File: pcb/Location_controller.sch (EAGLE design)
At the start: 41 parts, among them IC1 LIS302DL, X1 22-23-2021

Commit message: Further pcb layout routing
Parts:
- added DRN_POWER, RCM_POWER: (no value), pinhead:PINHD-1X2
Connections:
- removed net N$10: C9.1, POWER.1, REG.VOUT
- new net IN_3V: C8.1, POWER.2, REG.ENABLE, REG.VIN
- new net N$5: POWER.1, X1-1.S
- net GND: now also DRN_POWER.1, RCM_POWER.1
- net N$4: now also DRN_POWER.2, POWER.3; no longer C8.1, REG.ENABLE, REG.VIN, X1-1.S
- net VDD: now also C9.1, REG.VOUT; no longer POWER.2
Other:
- note added: "BATTERY"
- note added: "DRONE POWER"
- moved on the sheet: POWER, X1-1, X1-2

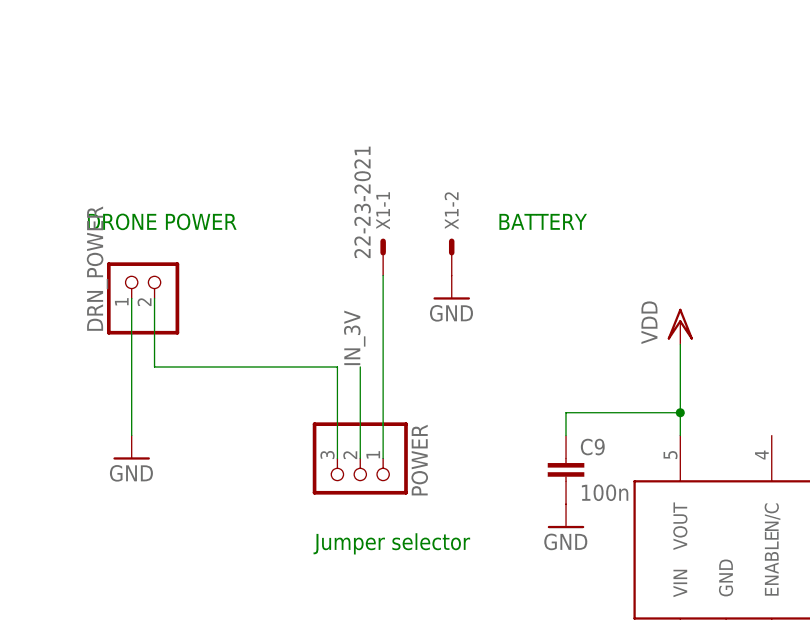
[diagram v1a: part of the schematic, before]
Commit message: Add barrel DC-jack to pcb
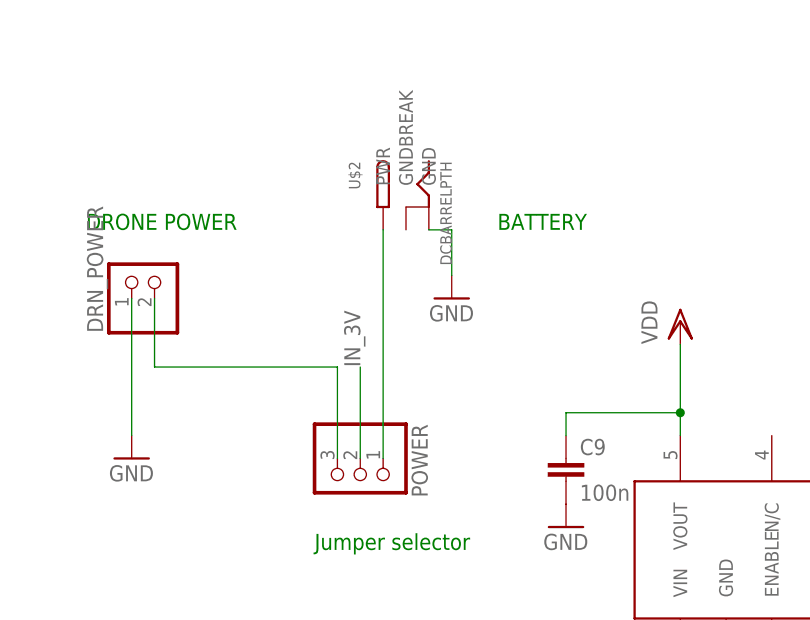
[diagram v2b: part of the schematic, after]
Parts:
- removed X1: 22-23-2021, con-molex:22-23-2021
- added U$2: DCBARRELPTH, BaseApp:DCBARRELPTH
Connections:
- net GND: now also U$2.GND; no longer X1-2.S
- net N$5: now also U$2.PWR; no longer X1-1.S
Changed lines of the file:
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@@
 <part name="C9" library="eagle-ltspice" deviceset="C" device="" value="100n"/>
 <part name="GND13" library="supply1" deviceset="GND" device=""/>
-<part name="X1" library="con-molex" deviceset="22-23-2021" device=""/>
 <part name="GND14" library="supply1" deviceset="GND" device=""/>
 <part name="GND15" library="supply1" deviceset="GND" device=""/>
@@
 <part name="RCM_POWER" library="pinhead" deviceset="PINHD-1X2" device=""/>
 <part name="GND19" library="supply1" deviceset="GND" device=""/>
+<part name="U$2" library="BaseApp" deviceset="DCBARREL" device="PTH"/>
 </parts>
 <sheets>
@@
 <instance part="C9" gate="G$1" x="-55.88" y="101.6"/>
 <instance part="GND13" gate="1" x="-55.88" y="93.98"/>
-<instance part="X1" gate="-1" x="-76.2" y="124.46" rot="R90"/>
-<instance part="X1" gate="-2" x="-68.58" y="124.46" rot="R90"/>
 <instance part="GND14" gate="1" x="-68.58" y="119.38"/>
 <instance part="GND15" gate="1" x="10.16" y="66.04"/>
@@
 <instance part="RCM_POWER" gate="G$1" x="-154.94" y="129.54" rot="R90"/>
 <instance part="GND19" gate="1" x="-157.48" y="119.38"/>
+<instance part="U$2" gate="G$1" x="-73.66" y="132.08" rot="MR270"/>
 </instances>
 <busses>
@@
 </segment>
 <segment>
-<pinref part="X1" gate="-2" pin="S"/>
-<pinref part="GND14" gate="1" pin="GND"/>
-</segment>
-<segment>
 <pinref part="GND18" gate="1" pin="GND"/>
 <pinref part="DRN_POWER" gate="G$1" pin="1"/>
@@
 <pinref part="GND19" gate="1" pin="GND"/>
 <wire x1="-157.48" y1="127" x2="-157.48" y2="121.92" width="0.1524" layer="91"/>
+</segment>
+<segment>
+<pinref part="U$2" gate="G$1" pin="GND"/>
+<pinref part="GND14" gate="1" pin="GND"/>
+<wire x1="-71.12" y1="127" x2="-68.58" y2="127" width="0.1524" layer="91"/>
+<wire x1="-68.58" y1="127" x2="-68.58" y2="121.92" width="0.1524" layer="91"/>
 </segment>
 </net>
@@
 <net name="N$5" class="0">
 <segment>
-<pinref part="X1" gate="-1" pin="S"/>
 <pinref part="POWER" gate="A" pin="1"/>
-<wire x1="-76.2" y1="121.92" x2="-76.2" y2="101.6" width="0.1524" layer="91"/>
-</segment>
-</net>
+<wire x1="-76.2" y1="127" x2="-76.2" y2="101.6" width="0.1524" layer="91"/>
+<pinref part="U$2" gate="G$1" pin="PWR"/>
+</segment>
+</net>

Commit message: Finish pcb routing
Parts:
- added JP1, JP3: (no value), pinhead:PINHD-1X6
- JP2: device pinhead:PINHD-1X20 -> pinhead:PINHD-1X6
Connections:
- net GND: now also JP1.1; no longer JP2.15
- net IN_3V: now also RCM_POWER.2
- net USART2_RX: now also JP1.5; no longer JP2.19
- net USART2_TX: now also JP1.4; no longer JP2.18
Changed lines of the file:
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@@
 <grid distance="0.1" unitdist="inch" unit="inch" style="lines" multiple="1" display="no" altdistance="0.01" altunitdist="inch" altunit="inch"/>
 <layers>
-<layer number="1" name="Top" color="4" fill="1" visible="no" active="no"/>
-<layer number="16" name="Bottom" color="1" fill="1" visible="no" active="no"/>
-<layer number="17" name="Pads" color="2" fill="1" visible="no" active="no"/>
-<layer number="18" name="Vias" color="2" fill="1" visible="no" active="no"/>
-<layer number="19" name="Unrouted" color="6" fill="1" visible="no" active="no"/>
-<layer number="20" name="Dimension" color="15" fill="1" visible="no" active="no"/>
-<layer number="21" name="tPlace" color="7" fill="1" visible="no" active="no"/>
-<layer number="22" name="bPlace" color="7" fill="1" visible="no" active="no"/>
-<layer number="23" name="tOrigins" color="15" fill="1" visible="no" active="no"/>
-<layer number="24" name="bOrigins" color="15" fill="1" visible="no" active="no"/>
-<layer number="25" name="tNames" color="7" fill="1" visible="no" active="no"/>
-<layer number="26" name="bNames" color="7" fill="1" visible="no" active="no"/>
-<layer number="27" name="tValues" color="7" fill="1" visible="no" active="no"/>
-<layer number="28" name="bValues" color="7" fill="1" visible="no" active="no"/>
+<layer number="1" name="Top" color="4" fill="1" visible="yes" active="no"/>
+<layer number="16" name="Bottom" color="1" fill="1" visible="yes" active="no"/>
+<layer number="17" name="Pads" color="2" fill="1" visible="yes" active="no"/>
+<layer number="18" name="Vias" color="2" fill="1" visible="yes" active="no"/>
+<layer number="19" name="Unrouted" color="6" fill="1" visible="yes" active="no"/>
+<layer number="20" name="Dimension" color="15" fill="1" visible="yes" active="no"/>
+<layer number="21" name="tPlace" color="7" fill="1" visible="yes" active="no"/>
+<layer number="22" name="bPlace" color="7" fill="1" visible="yes" active="no"/>
+<layer number="23" name="tOrigins" color="15" fill="1" visible="yes" active="no"/>
+<layer number="24" name="bOrigins" color="15" fill="1" visible="yes" active="no"/>
+<layer number="25" name="tNames" color="7" fill="1" visible="yes" active="no"/>
+<layer number="26" name="bNames" color="7" fill="1" visible="yes" active="no"/>
+<layer number="27" name="tValues" color="7" fill="1" visible="yes" active="no"/>
+<layer number="28" name="bValues" color="7" fill="1" visible="yes" active="no"/>
 <layer number="29" name="tStop" color="7" fill="3" visible="no" active="no"/>
 <layer number="30" name="bStop" color="7" fill="6" visible="no" active="no"/>
@@
 <layer number="35" name="tGlue" color="7" fill="4" visible="no" active="no"/>
 <layer number="36" name="bGlue" color="7" fill="5" visible="no" active="no"/>
-<layer number="37" name="tTest" color="7" fill="1" visible="no" active="no"/>
-<layer number="38" name="bTest" color="7" fill="1" visible="no" active="no"/>
+<layer number="37" name="tTest" color="7" fill="1" visible="yes" active="no"/>
+<layer number="38" name="bTest" color="7" fill="1" visible="yes" active="no"/>
 <layer number="39" name="tKeepout" color="4" fill="11" visible="no" active="no"/>
 <layer number="40" name="bKeepout" color="1" fill="11" visible="no" active="no"/>
@@
 <layer number="44" name="Drills" color="7" fill="1" visible="no" active="no"/>
 <layer number="45" name="Holes" color="7" fill="1" visible="no" active="no"/>
-<layer number="46" name="Milling" color="3" fill="1" visible="no" active="no"/>
-<layer number="47" name="Measures" color="7" fill="1" visible="no" active="no"/>
-<layer number="48" name="Document" color="7" fill="1" visible="no" active="no"/>
-<layer number="49" name="Reference" color="7" fill="1" visible="no" active="no"/>
-<layer number="50" name="dxf" color="7" fill="1" visible="no" active="no"/>
-<layer number="51" name="tDocu" color="7" fill="1" visible="no" active="no"/>
-<layer number="52" name="bDocu" color="7" fill="1" visible="no" active="no"/>
-<layer number="53" name="tGND_GNDA" color="7" fill="9" visible="no" active="no"/>
-<layer number="54" name="bGND_GNDA" color="1" fill="9" visible="no" active="no"/>
-<layer number="56" name="wert" color="7" fill="1" visible="no" active="no"/>
-<layer number="57" name="tCAD" color="10" fill="1" visible="no" active="no"/>
-<layer number="58" name="bCAD" color="11" fill="1" visible="no" active="no"/>
+<layer number="46" name="Milling" color="3" fill="1" visible="yes" active="no"/>
+<layer number="47" name="Measures" color="7" fill="1" visible="yes" active="no"/>
+<layer number="48" name="Document" color="7" fill="1" visible="yes" active="no"/>
+<layer number="49" name="Reference" color="7" fill="1" visible="yes" active="no"/>
+<layer number="50" name="dxf" color="7" fill="1" visible="yes" active="no"/>
+<layer number="51" name="tDocu" color="7" fill="1" visible="yes" active="no"/>
+<layer number="52" name="bDocu" color="7" fill="1" visible="yes" active="no"/>
+<layer number="53" name="tGND_GNDA" color="7" fill="9" visible="yes" active="no"/>
+<layer number="54" name="bGND_GNDA" color="1" fill="9" visible="yes" active="no"/>
+<layer number="56" name="wert" color="7" fill="1" visible="yes" active="no"/>
+<layer number="57" name="tCAD" color="10" fill="1" visible="yes" active="no"/>
+<layer number="58" name="bCAD" color="11" fill="1" visible="yes" active="no"/>
 <layer number="91" name="Nets" color="2" fill="1" visible="yes" active="yes"/>
 <layer number="92" name="Busses" color="1" fill="1" visible="yes" active="yes"/>
@@
 <part name="GND6" library="supply1" deviceset="GND" device=""/>
 <part name="POWER" library="pinhead" deviceset="PINHD-1X3" device=""/>
-<part name="JP2" library="pinhead" deviceset="PINHD-1X20" device=""/>
 <part name="GND7" library="supply1" deviceset="GND" device=""/>
 <part name="VDD2" library="supply1" deviceset="VDD" device=""/>
@@
 <part name="GND19" library="supply1" deviceset="GND" device=""/>
 <part name="U$2" library="BaseApp" deviceset="DCBARREL" device="PTH"/>
+<part name="JP1" library="pinhead" deviceset="PINHD-1X6" device=""/>
+<part name="JP2" library="pinhead" deviceset="PINHD-1X6" device=""/>
+<part name="JP3" library="pinhead" deviceset="PINHD-1X6" device=""/>
 </parts>
 <sheets>
@@
 <instance part="GND6" gate="1" x="27.94" y="142.24" rot="R180"/>
 <instance part="POWER" gate="A" x="-78.74" y="99.06" rot="R270"/>
-<instance part="JP2" gate="A" x="-50.8" y="-60.96" rot="R90"/>
-<instance part="GND7" gate="1" x="-38.1" y="-81.28"/>
+<instance part="GND7" gate="1" x="-40.64" y="-81.28"/>
 <instance part="VDD2" gate="G$1" x="152.4" y="-7.62" rot="R270"/>
 <instance part="R5" gate="G$1" x="139.7" y="-7.62" rot="R180"/>
@@
 <instance part="GND19" gate="1" x="-157.48" y="119.38"/>
 <instance part="U$2" gate="G$1" x="-73.66" y="132.08" rot="MR270"/>
+<instance part="JP1" gate="A" x="-33.02" y="-60.96" rot="R90"/>
+<instance part="JP2" gate="A" x="-55.88" y="-60.96" rot="R90"/>
+<instance part="JP3" gate="A" x="-78.74" y="-60.96" rot="R90"/>
 </instances>
 <busses>
@@
 </segment>
 <segment>
-<pinref part="JP2" gate="A" pin="15"/>
-<wire x1="-38.1" y1="-63.5" x2="-38.1" y2="-78.74" width="0.1524" layer="91"/>
-<pinref part="GND7" gate="1" pin="GND"/>
-</segment>
-<segment>
 <pinref part="SWD" gate="A" pin="3"/>
 <pinref part="GND17" gate="1" pin="GND"/>
@@
 <wire x1="-71.12" y1="127" x2="-68.58" y2="127" width="0.1524" layer="91"/>
 <wire x1="-68.58" y1="127" x2="-68.58" y2="121.92" width="0.1524" layer="91"/>
+</segment>
+<segment>
+<pinref part="GND7" gate="1" pin="GND"/>
+<pinref part="JP1" gate="A" pin="1"/>
+<wire x1="-40.64" y1="-78.74" x2="-40.64" y2="-63.5" width="0.1524" layer="91"/>
 </segment>
 </net>
@@
 </segment>
 <segment>
-<pinref part="JP2" gate="A" pin="18"/>
-<wire x1="-30.48" y1="-63.5" x2="-30.48" y2="-78.74" width="0.1524" layer="91"/>
-<label x="-30.48" y="-83.82" size="1.778" layer="95" rot="R90"/>
+<pinref part="JP1" gate="A" pin="4"/>
+<wire x1="-33.02" y1="-63.5" x2="-33.02" y2="-78.74" width="0.1524" layer="91"/>
+<label x="-33.02" y="-78.74" size="1.778" layer="95" rot="R90"/>
 </segment>
 </net>
@@
 </segment>
 <segment>
-<pinref part="JP2" gate="A" pin="19"/>
-<wire x1="-27.94" y1="-63.5" x2="-27.94" y2="-78.74" width="0.1524" layer="91"/>
-<label x="-25.4" y="-83.82" size="1.778" layer="95" rot="R90"/>
+<pinref part="JP1" gate="A" pin="5"/>
+<wire x1="-30.48" y1="-63.5" x2="-30.48" y2="-78.74" width="0.1524" layer="91"/>
+<label x="-30.48" y="-78.74" size="1.778" layer="95" rot="R90"/>
 </segment>
 </net>
@@
 <label x="-50.8" y="76.2" size="1.778" layer="95"/>
 </segment>
-</net>
+<segment>
+<pinref part="RCM_POWER" gate="G$1" pin="2"/>
+<wire x1="-154.94" y1="127" x2="-154.94" y2="121.92" width="0.1524" layer="91"/>
+<wire x1="-154.94" y1="121.92" x2="-149.86" y2="121.92" width="0.1524" layer="91"/>
+<wire x1="-149.86" y1="121.92" x2="-149.86" y2="114.3" width="0.1524" layer="91"/>
+<label x="-149.86" y="114.3" size="1.778" layer="95" rot="R90"/>
+</segment>
+</net>
